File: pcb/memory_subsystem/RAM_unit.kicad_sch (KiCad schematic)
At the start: 6 parts, among them U3 74LS245

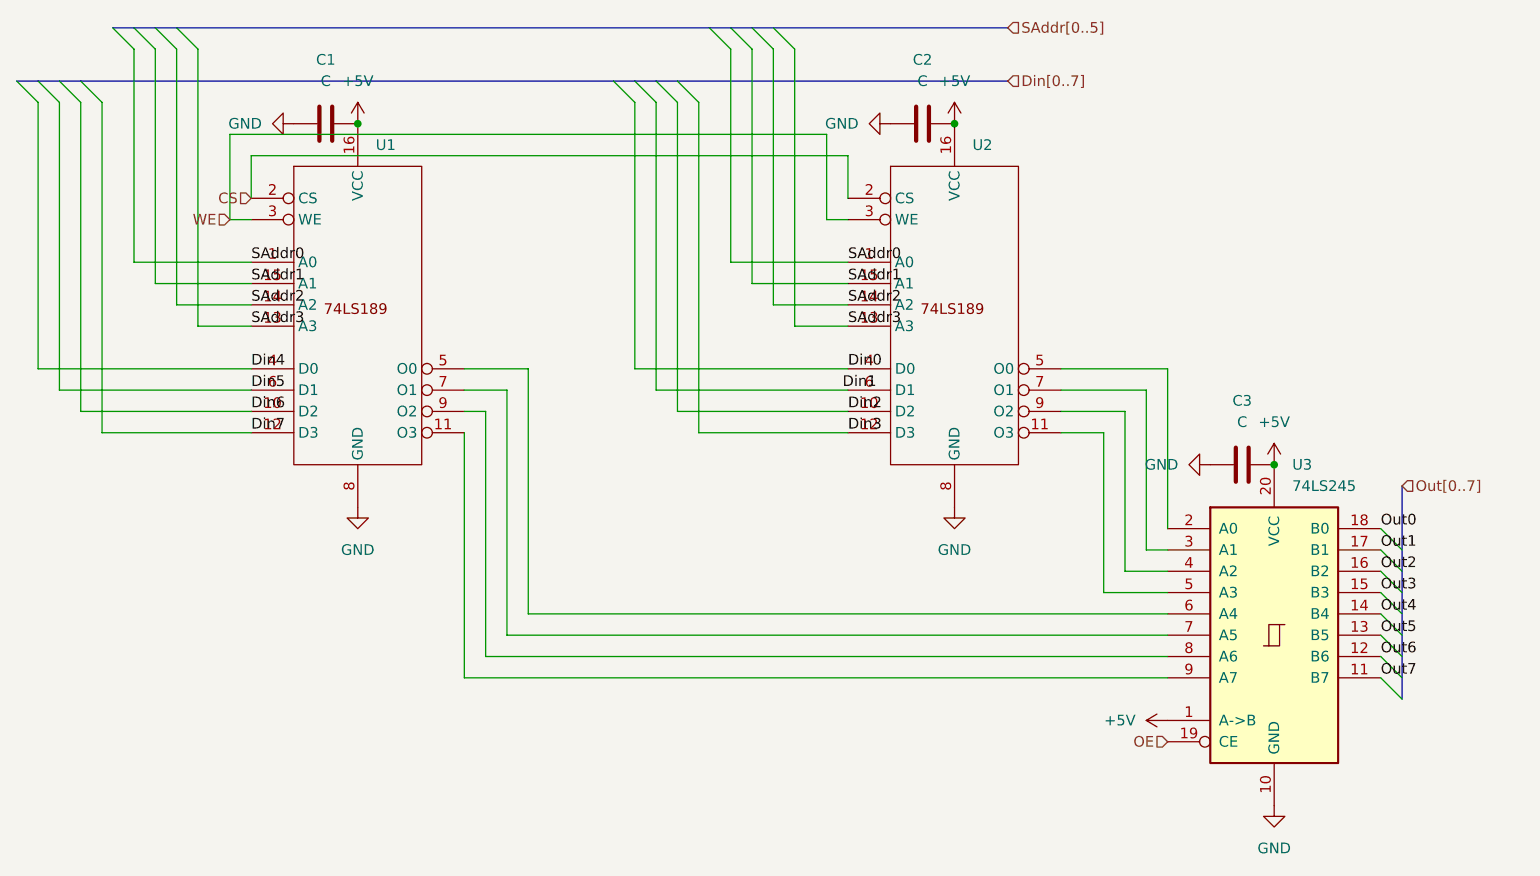
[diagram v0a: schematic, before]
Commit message: Fixed spacing problem: no warnings/erros
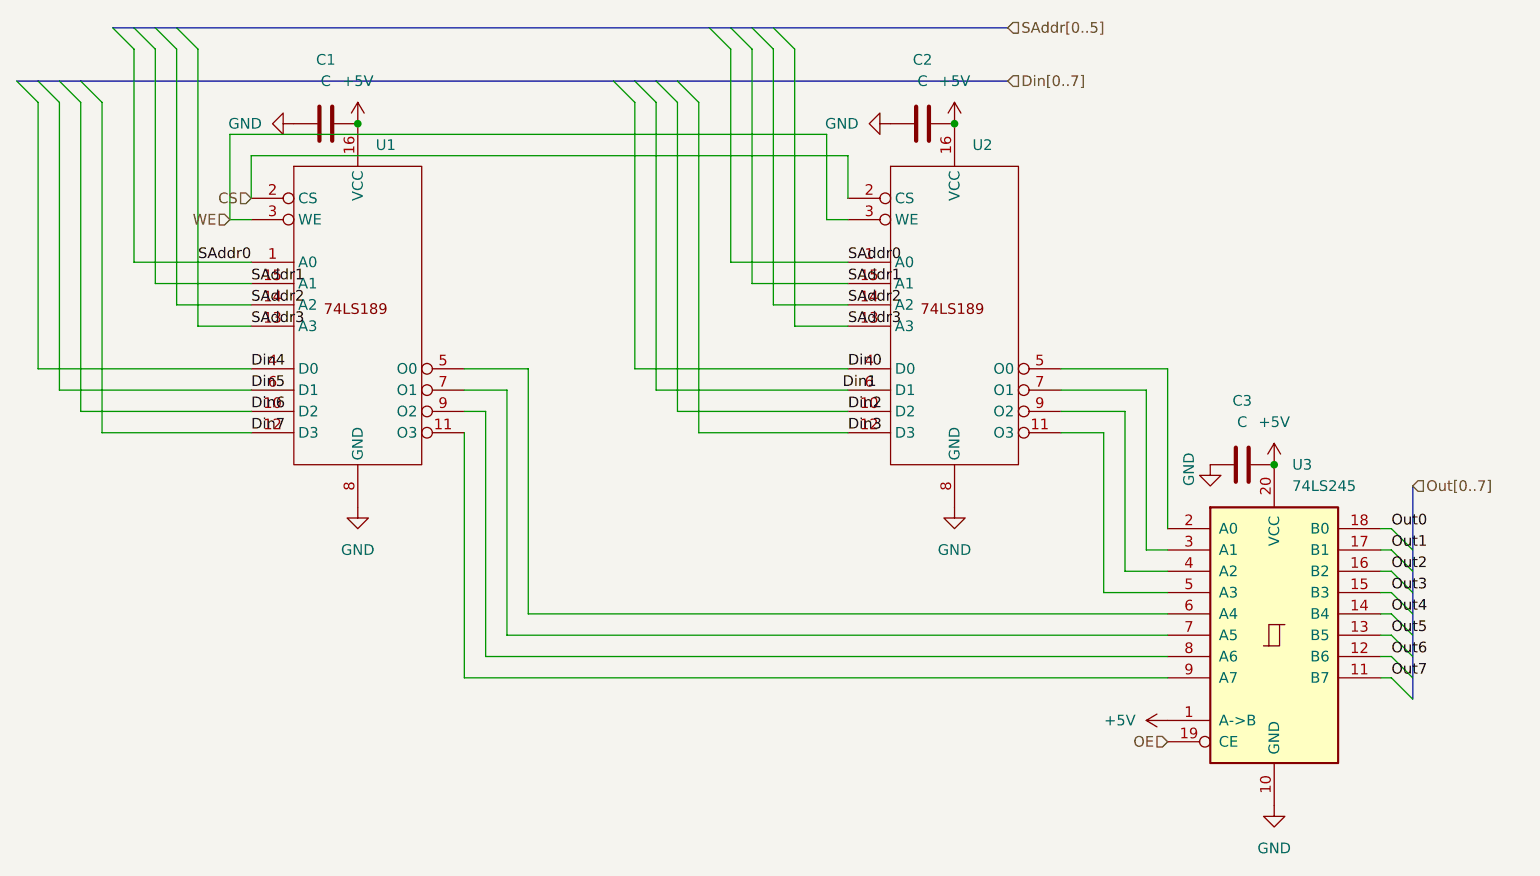
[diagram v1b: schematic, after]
